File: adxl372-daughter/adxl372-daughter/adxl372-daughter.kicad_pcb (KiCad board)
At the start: 2 copper layers, 30.5 x 23.4 mm, 13 parts, among them J1 Conn_01x08, J2 Conn_01x08, J3 Conn_01x05_Female, J4 Conn_01x05_Female, U1 ADXL372

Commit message: fleshed out daughter card
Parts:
- removed ?: , 
- removed REF** (x4): MountingHole_3mm, MountingHole:MountingHole_3mm
- added H1: MountingHole_3mm_Pad, MountingHole:MountingHole_3mm_Pad, F.Cu at (117.6, 54.1)
- added H2: MountingHole_3mm_Pad, MountingHole:MountingHole_3mm_Pad, F.Cu at (149.1, 54.1)
- added H3: MountingHole_3mm_Pad, MountingHole:MountingHole_3mm_Pad, F.Cu at (149.1, 72.9)
- added H4: MountingHole_3mm_Pad, MountingHole:MountingHole_3mm_Pad, F.Cu at (117.6, 72.9)
- added JP1: SolderJumper_2_Bridged, Jumper:SolderJumper-2_P1.3mm_Bridged2Bar_Pad1.0x1.5mm, F.Cu at (127.5, 63.5)
- added JP2: SolderJumper_3_Bridged12, Jumper:SolderJumper-3_P1.3mm_Bridged2Bar12_Pad1.0x1.5mm, F.Cu at (124.2, 66.0)
- added JP3: SolderJumper_3_Bridged12, Jumper:SolderJumper-3_P1.3mm_Bridged2Bar12_Pad1.0x1.5mm, F.Cu at (124.2, 61.0)
- added R1: 0, Resistor_SMD:R_0603_1608Metric_Pad1.05x0.95mm_HandSolder, F.Cu at (133.9, 67.8)
- added R2: 0, Resistor_SMD:R_0603_1608Metric_Pad1.05x0.95mm_HandSolder, F.Cu at (128.5, 67.8)
- added R3: 0, Resistor_SMD:R_0603_1608Metric_Pad1.05x0.95mm_HandSolder, F.Cu at (130.3, 67.8)
- added R4: 0, Resistor_SMD:R_0603_1608Metric_Pad1.05x0.95mm_HandSolder, F.Cu at (132.1, 67.8)
- moved C3 43.2 mm to (131.1, 59.7), turned to 270 degrees
- moved J3 38.3 mm to (137.4, 58.4)
- moved J4 38.3 mm to (145.0, 58.4)
- moved J2 37.0 mm to (148.8, 63.5)
- moved C2 36.2 mm to (132.8, 59.7)
- moved C1 36.1 mm to (134.6, 59.7)
- moved U1 36.1 mm to (133.3, 63.5)
- moved J1 35.7 mm to (117.8, 63.5)
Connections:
- J4 pad 2: SCLK -> rSCLK
- J4 pad 3: MOSI -> rMOSI
- J4 pad 4: MISO -> rMISO
- J4 pad 5: nCS -> rnCS
- U1 pad 4: SCLK -> rSCLK
- U1 pad 6: MOSI -> rMOSI
- U1 pad 7: MISO -> rMISO
- U1 pad 8: nCS -> rnCS
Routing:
- net rMOSI: track 0.00 -> 39.6 mm, vias 0 -> 1
- net rSCLK: track 0.00 -> 28.2 mm, vias 0 -> 1
- net dnCS: track 0.00 -> 25.9 mm
- net VDD: track 86.5 -> 63.2 mm
- net rMISO: track 0.00 -> 22.7 mm
- net MOSI: track 43.3 -> 65.7 mm
- net INT2: track 10.7 -> 31.2 mm, vias 1 -> 2
- net D1: track 28.6 -> 47.6 mm, vias 2 -> 0
- net GND: track 29.9 -> 11.4 mm, vias 30 -> 10
- net D2: track 29.2 -> 44.8 mm
- net rnCS: track 0.00 -> 15.2 mm
- net SCLK: track 34.5 -> 46.3 mm, vias 3 -> 4
- net MISO: track 39.6 -> 50.6 mm, vias 2 -> 4
- net INT1: track 9.42 -> 19.6 mm
- net nCS: track 44.9 -> 46.3 mm, vias 2 -> 4
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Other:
- board size 30.5 x 23.4 mm -> 38.1 x 25.4 mm
- board text added: "CS"
- board text added: "D1"
- board text added: "D2"
- board text added: "INPUT"
- board text added: "INT1"
- board text added: "INT2"
- board text added: "OUTPUT"
- board text added: "nCS"
- board text removed: "IN"

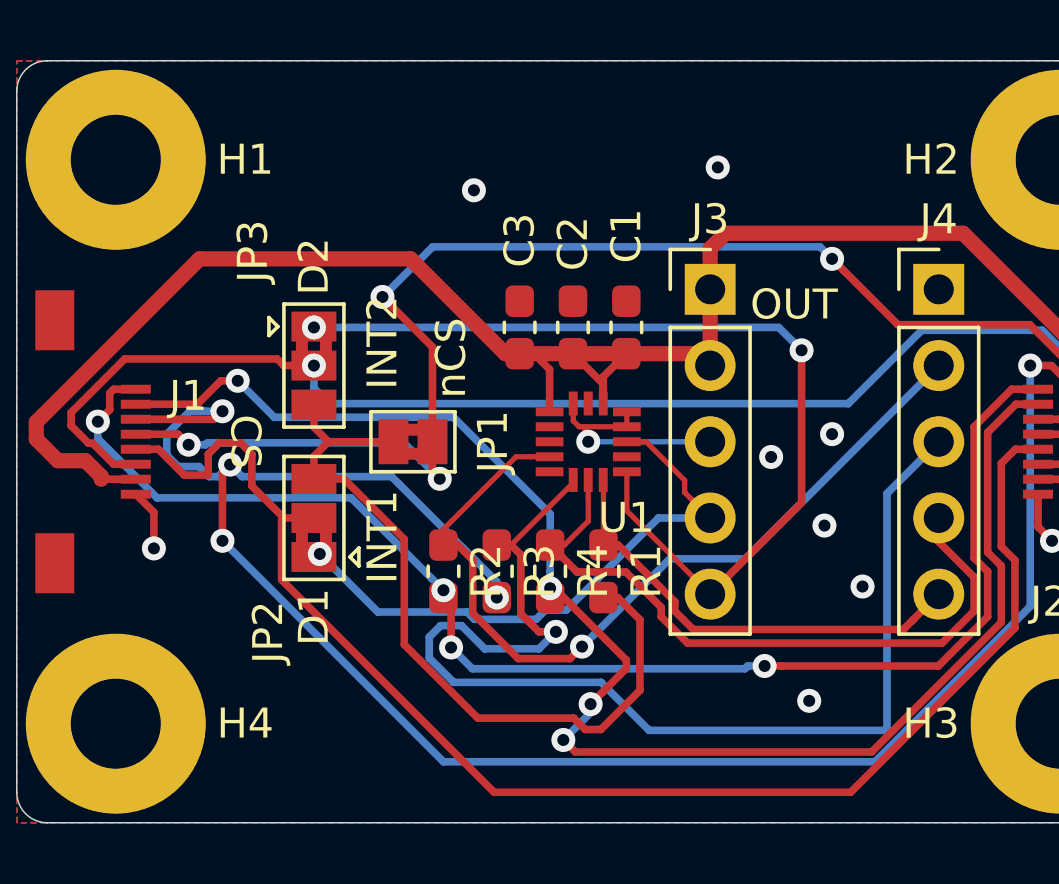
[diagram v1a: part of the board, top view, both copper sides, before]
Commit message: improved ground conectivity
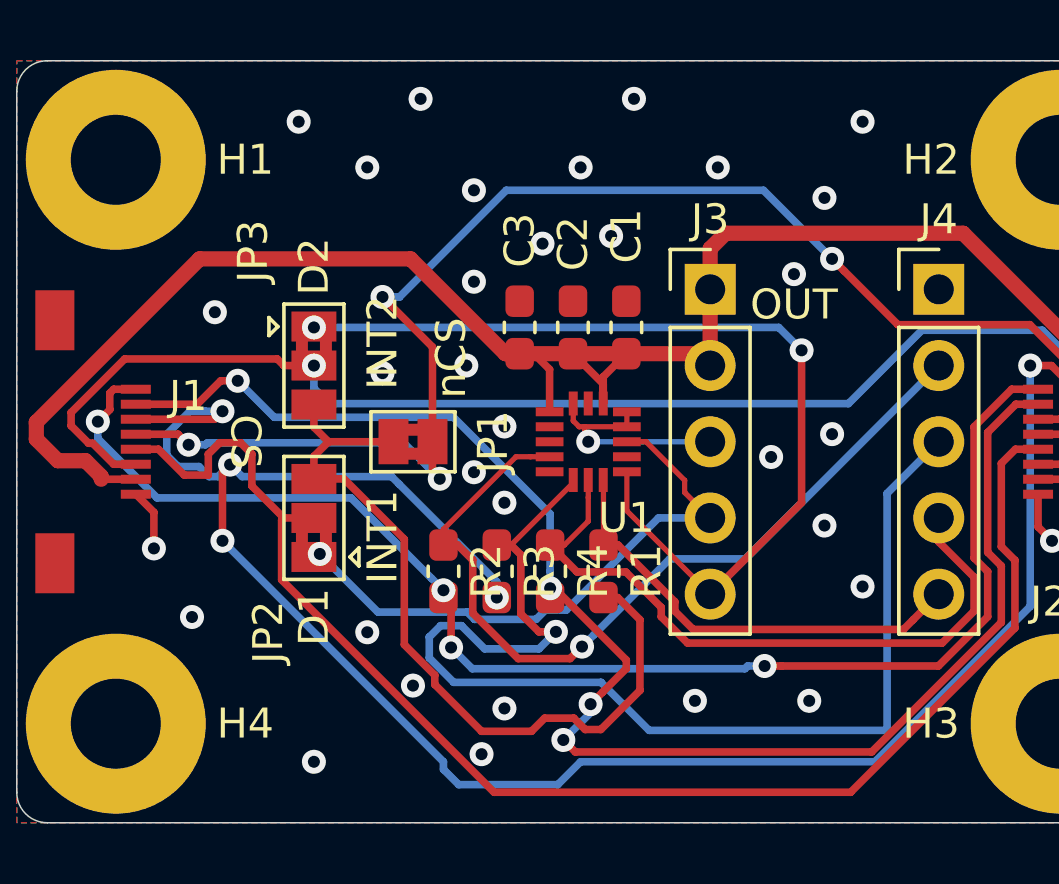
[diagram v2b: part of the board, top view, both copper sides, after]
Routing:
- net nCS: track 46.3 -> 47.9 mm
- net MOSI: track 65.7 -> 66.5 mm
- net dnCS: track 25.9 -> 26.4 mm
- net GND: vias 10 -> 34
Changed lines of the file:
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@@
     (thickness 1.6)
     (drawings 18)
-    (tracks 305)
+    (tracks 339)
     (zones 0)
     (modules 19)
@@
   )
   (setup
-    (last_trace_width 0.25)
+    (last_trace_width 0.254)
     (user_trace_width 0.1524)
     (user_trace_width 0.1778)
@@
     (user_trace_width 0.508)
     (trace_clearance 0.2)
-    (zone_clearance 0.508)
+    (zone_clearance 0.254)
     (zone_45_only no)
     (trace_min 0.1524)
@@
   (gr_arc (start 115.316 75.184) (end 114.3 75.184) (angle -90) (layer Edge.Cuts) (width 0.05))
   (gr_arc (start 151.384 51.816) (end 152.4 51.816) (angle -90) (layer Edge.Cuts) (width 0.05))
+  (via (at 129.54 64.516) (size 0.8) (drill 0.4) (layers F.Cu B.Cu) (net 1))
+  (via (at 130.556 65.532) (size 0.8) (drill 0.4) (layers F.Cu B.Cu) (net 1))
   (segment (start 134.6375 62.5) (end 134.6375 63) (width 0.1778) (layer F.Cu) (net 1))
   (segment (start 132.85 62.8028) (end 132.85 62.225) (width 0.1778) (layer F.Cu) (net 1))
@@
   (via (at 148.80901 66.802) (size 0.8) (drill 0.4) (layers F.Cu B.Cu) (net 1))
   (segment (start 148.344 65.25) (end 148.344 66.33699) (width 0.254) (layer F.Cu) (net 1))
+  (via (at 120.904 59.182) (size 0.8) (drill 0.4) (layers F.Cu B.Cu) (net 1))
+  (via (at 123.698 52.832) (size 0.8) (drill 0.4) (layers F.Cu B.Cu) (net 1))
+  (via (at 125.984 69.85) (size 0.8) (drill 0.4) (layers F.Cu B.Cu) (net 1))
+  (via (at 127.508 71.628) (size 0.8) (drill 0.4) (layers F.Cu B.Cu) (net 1))
+  (via (at 130.556 62.992) (size 0.8) (drill 0.4) (layers F.Cu B.Cu) (net 1))
+  (via (at 129.286 60.96) (size 0.8) (drill 0.4) (layers F.Cu B.Cu) (net 1))
+  (via (at 129.54 58.166) (size 0.8) (drill 0.4) (layers F.Cu B.Cu) (net 1))
+  (via (at 133.096 54.356) (size 0.8) (drill 0.4) (layers F.Cu B.Cu) (net 1))
+  (via (at 127.762 52.07) (size 0.8) (drill 0.4) (layers F.Cu B.Cu) (net 1))
+  (via (at 125.984 54.356) (size 0.8) (drill 0.4) (layers F.Cu B.Cu) (net 1))
+  (via (at 142.494 52.832) (size 0.8) (drill 0.4) (layers F.Cu B.Cu) (net 1))
+  (via (at 141.224 55.372) (size 0.8) (drill 0.4) (layers F.Cu B.Cu) (net 1))
+  (via (at 134.874 52.07) (size 0.8) (drill 0.4) (layers F.Cu B.Cu) (net 1))
+  (via (at 140.208 57.912) (size 0.8) (drill 0.4) (layers F.Cu B.Cu) (net 1))
+  (via (at 134.112 56.642) (size 0.8) (drill 0.4) (layers F.Cu B.Cu) (net 1))
+  (via (at 131.826 56.896) (size 0.8) (drill 0.4) (layers F.Cu B.Cu) (net 1))
+  (via (at 124.206 74.168) (size 0.8) (drill 0.4) (layers F.Cu B.Cu) (net 1))
+  (via (at 120.142 69.342) (size 0.8) (drill 0.4) (layers F.Cu B.Cu) (net 1))
+  (via (at 129.794 73.914) (size 0.8) (drill 0.4) (layers F.Cu B.Cu) (net 1))
+  (via (at 130.556 72.39) (size 0.8) (drill 0.4) (layers F.Cu B.Cu) (net 1))
+  (via (at 136.906 72.136) (size 0.8) (drill 0.4) (layers F.Cu B.Cu) (net 1))
+  (via (at 126.492 61.214) (size 0.8) (drill 0.4) (layers F.Cu B.Cu) (net 1))
   (segment (start 133.85 61.335) (end 134.62 60.565) (width 0.254) (layer F.Cu) (net 2))
   (segment (start 133.85 62.225) (end 133.85 61.335) (width 0.254) (layer F.Cu) (net 2))
@@
   (segment (start 148.082 68.990038) (end 142.904038 74.168) (width 0.254) (layer B.Cu) (net 5))
   (via (at 121.158 66.802) (size 0.8) (drill 0.4) (layers F.Cu B.Cu) (net 5))
-  (segment (start 142.904038 74.168) (end 128.524 74.168) (width 0.254) (layer B.Cu) (net 5))
   (segment (start 128.524 74.168) (end 121.158 66.802) (width 0.254) (layer B.Cu) (net 5))
   (via (at 121.412 64.262) (size 0.8) (drill 0.4) (layers F.Cu B.Cu) (net 5))
@@
   (segment (start 126.795999 64.661999) (end 127.050022 64.916022) (width 0.254) (layer B.Cu) (net 5))
   (segment (start 121.412 64.262) (end 121.811999 64.661999) (width 0.254) (layer B.Cu) (net 5))
+  (segment (start 128.524 74.168) (end 128.524 74.422) (width 0.254) (layer B.Cu) (net 5))
+  (segment (start 128.524 74.422) (end 129.032 74.93) (width 0.254) (layer B.Cu) (net 5))
+  (segment (start 132.334 74.93) (end 133.096 74.168) (width 0.254) (layer B.Cu) (net 5))
+  (segment (start 129.032 74.93) (end 132.334 74.93) (width 0.254) (layer B.Cu) (net 5))
+  (segment (start 142.904038 74.168) (end 133.096 74.168) (width 0.254) (layer B.Cu) (net 5))
   (segment (start 128.158 64.504) (end 128.38901 64.73501) (width 0.254) (layer F.Cu) (net 6))
   (segment (start 128.158 63.5) (end 128.158 64.504) (width 0.254) (layer F.Cu) (net 6))
@@
   (via (at 141.478 57.404) (size 0.8) (drill 0.4) (layers F.Cu B.Cu) (net 6))
   (via (at 126.492 58.674) (size 0.8) (drill 0.4) (layers F.Cu B.Cu) (net 6))
-  (segment (start 128.161999 57.004001) (end 126.492 58.674) (width 0.254) (layer B.Cu) (net 6))
-  (segment (start 141.078001 57.004001) (end 128.161999 57.004001) (width 0.254) (layer B.Cu) (net 6))
-  (segment (start 141.478 57.404) (end 141.078001 57.004001) (width 0.254) (layer B.Cu) (net 6))
   (segment (start 128.158 60.34) (end 128.158 63.5) (width 0.254) (layer F.Cu) (net 6))
   (segment (start 126.492 58.674) (end 128.158 60.34) (width 0.254) (layer F.Cu) (net 6))
@@
   (segment (start 127.200837 63.534999) (end 120.659479 63.534999) (width 0.254) (layer B.Cu) (net 6))
   (segment (start 120.659479 63.534999) (end 120.594555 63.599923) (width 0.254) (layer B.Cu) (net 6))
+  (segment (start 141.478 57.404) (end 139.192 55.118) (width 0.254) (layer B.Cu) (net 6))
+  (segment (start 130.615962 55.118) (end 127.059962 58.674) (width 0.254) (layer B.Cu) (net 6))
+  (segment (start 127.057685 58.674) (end 126.492 58.674) (width 0.254) (layer B.Cu) (net 6))
+  (segment (start 127.059962 58.674) (end 127.057685 58.674) (width 0.254) (layer B.Cu) (net 6))
+  (segment (start 139.192 55.118) (end 130.615962 55.118) (width 0.254) (layer B.Cu) (net 6))
   (segment (start 147.57303 69.709134) (end 142.098164 75.184) (width 0.254) (layer F.Cu) (net 7))
   (segment (start 147.573031 67.450869) (end 147.57303 69.709134) (width 0.254) (layer F.Cu) (net 7))
@@
   (segment (start 124.692 63.5) (end 124.206 63.986) (width 0.254) (layer F.Cu) (net 15))
   (segment (start 126.858 63.5) (end 124.692 63.5) (width 0.254) (layer F.Cu) (net 15))
-  (segment (start 127.219001 70.263039) (end 129.669951 72.713989) (width 0.254) (layer F.Cu) (net 15))
-  (segment (start 132.868787 72.713989) (end 133.246827 73.092029) (width 0.254) (layer F.Cu) (net 15))
   (segment (start 134.333 68.693) (end 133.858 68.693) (width 0.254) (layer F.Cu) (net 15))
   (segment (start 133.77116 73.092029) (end 135.074011 71.789178) (width 0.254) (layer F.Cu) (net 15))
-  (segment (start 124.206 64.74) (end 125.21 64.74) (width 0.254) (layer F.Cu) (net 15))
   (segment (start 135.074011 69.434011) (end 134.333 68.693) (width 0.254) (layer F.Cu) (net 15))
   (segment (start 125.21 64.74) (end 127.219001 66.749001) (width 0.254) (layer F.Cu) (net 15))
+  (segment (start 127.219001 70.263039) (end 128.235001 71.279039) (width 0.254) (layer F.Cu) (net 15))
+  (segment (start 135.074011 71.789178) (end 135.074011 69.434011) (width 0.254) (layer F.Cu) (net 15))
+  (segment (start 131.457978 73.152) (end 131.895989 72.713989) (width 0.254) (layer F.Cu) (net 15))
+  (segment (start 132.868787 72.713989) (end 133.246827 73.092029) (width 0.254) (layer F.Cu) (net 15))
   (segment (start 127.219001 66.749001) (end 127.219001 70.263039) (width 0.254) (layer F.Cu) (net 15))
-  (segment (start 135.074011 71.789178) (end 135.074011 69.434011) (width 0.254) (layer F.Cu) (net 15))
+  (segment (start 124.206 64.74) (end 125.21 64.74) (width 0.254) (layer F.Cu) (net 15))
+  (segment (start 128.235001 71.279039) (end 128.235001 71.593001) (width 0.254) (layer F.Cu) (net 15))
   (segment (start 133.246827 73.092029) (end 133.77116 73.092029) (width 0.254) (layer F.Cu) (net 15))
-  (segment (start 129.669951 72.713989) (end 132.868787 72.713989) (width 0.254) (layer F.Cu) (net 15))
+  (segment (start 128.235001 71.593001) (end 129.794 73.152) (width 0.254) (layer F.Cu) (net 15))
+  (segment (start 129.794 73.152) (end 131.457978 73.152) (width 0.254) (layer F.Cu) (net 15))
+  (segment (start 131.895989 72.713989) (end 132.868787 72.713989) (width 0.254) (layer F.Cu) (net 15))
   (zone (net 1) (net_name GND) (layer B.Cu) (hatch edge 0.508)
-    (connect_pads (clearance 0.508))
-    (min_thickness 0.254)
+    (connect_pads (clearance 0.254))
+    (min_thickness 0.1778)
     (fill yes (arc_segments 32) (thermal_gap 0.508) (thermal_bridge_width 0.508))
     (polygon
@@
   )
   (zone (net 1) (net_name GND) (layer F.Cu) (hatch edge 0.508)
-    (connect_pads (clearance 0.508))
-    (min_thickness 0.254)
+    (connect_pads (clearance 0.254))
+    (min_thickness 0.1778)
     (fill yes (arc_segments 32) (thermal_gap 0.508) (thermal_bridge_width 0.508))
     (polygon

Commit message: make pass drc
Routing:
- net D1: track 47.6 -> 48.9 mm
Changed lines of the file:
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@@
     (thickness 1.6)
     (drawings 18)
-    (tracks 339)
+    (tracks 338)
     (zones 0)
     (modules 19)
@@
   (via (at 123.698 52.832) (size 0.8) (drill 0.4) (layers F.Cu B.Cu) (net 1))
   (via (at 125.984 69.85) (size 0.8) (drill 0.4) (layers F.Cu B.Cu) (net 1))
-  (via (at 127.508 71.628) (size 0.8) (drill 0.4) (layers F.Cu B.Cu) (net 1))
+  (via (at 127.508 71.882) (size 0.8) (drill 0.4) (layers F.Cu B.Cu) (net 1))
   (via (at 130.556 62.992) (size 0.8) (drill 0.4) (layers F.Cu B.Cu) (net 1))
   (via (at 129.286 60.96) (size 0.8) (drill 0.4) (layers F.Cu B.Cu) (net 1))
@@
   (via (at 124.206 74.168) (size 0.8) (drill 0.4) (layers F.Cu B.Cu) (net 1))
   (via (at 120.142 69.342) (size 0.8) (drill 0.4) (layers F.Cu B.Cu) (net 1))
-  (via (at 129.794 73.914) (size 0.8) (drill 0.4) (layers F.Cu B.Cu) (net 1))
+  (via (at 129.286 73.914) (size 0.8) (drill 0.4) (layers F.Cu B.Cu) (net 1))
   (via (at 130.556 72.39) (size 0.8) (drill 0.4) (layers F.Cu B.Cu) (net 1))
   (via (at 136.906 72.136) (size 0.8) (drill 0.4) (layers F.Cu B.Cu) (net 1))
@@
   (segment (start 127.059962 58.674) (end 127.057685 58.674) (width 0.254) (layer B.Cu) (net 6))
   (segment (start 139.192 55.118) (end 130.615962 55.118) (width 0.254) (layer B.Cu) (net 6))
-  (segment (start 147.57303 69.709134) (end 142.098164 75.184) (width 0.254) (layer F.Cu) (net 7))
-  (segment (start 147.573031 67.450869) (end 147.57303 69.709134) (width 0.254) (layer F.Cu) (net 7))
-  (segment (start 147.119022 66.996861) (end 147.573031 67.450869) (width 0.254) (layer F.Cu) (net 7))
-  (segment (start 147.119022 64.220978) (end 147.119022 66.996861) (width 0.254) (layer F.Cu) (net 7))
-  (segment (start 148.344 63.75) (end 147.59 63.75) (width 0.254) (layer F.Cu) (net 7))
-  (segment (start 147.59 63.75) (end 147.119022 64.220978) (width 0.254) (layer F.Cu) (net 7))
-  (segment (start 123.128999 68.101601) (end 123.128999 66.113001) (width 0.254) (layer F.Cu) (net 7))
   (segment (start 123.202 66.04) (end 124.206 66.04) (width 0.254) (layer F.Cu) (net 7))
-  (segment (start 123.128999 66.113001) (end 123.202 66.04) (width 0.254) (layer F.Cu) (net 7))
-  (segment (start 130.211398 75.184) (end 123.128999 68.101601) (width 0.254) (layer F.Cu) (net 7))
-  (segment (start 142.098164 75.184) (end 130.211398 75.184) (width 0.254) (layer F.Cu) (net 7))
   (segment (start 120.684998 63.913038) (end 121.063038 63.534998) (width 0.254) (layer F.Cu) (net 7))
   (segment (start 120.684998 64.610962) (end 120.684998 63.913038) (width 0.254) (layer F.Cu) (net 7))
@@
   (segment (start 118.27 63.75) (end 119.024 63.75) (width 0.254) (layer F.Cu) (net 7))
   (segment (start 122.139002 63.913038) (end 122.139002 64.977002) (width 0.254) (layer F.Cu) (net 7))
+  (segment (start 128.016 75.184) (end 123.128999 70.296999) (width 0.254) (layer F.Cu) (net 7))
+  (segment (start 142.098164 75.184) (end 128.016 75.184) (width 0.254) (layer F.Cu) (net 7))
+  (segment (start 147.57303 69.709134) (end 142.098164 75.184) (width 0.254) (layer F.Cu) (net 7))
+  (segment (start 147.119022 66.996861) (end 147.573031 67.450869) (width 0.254) (layer F.Cu) (net 7))
+  (segment (start 123.128999 66.113001) (end 123.202 66.04) (width 0.254) (layer F.Cu) (net 7))
+  (segment (start 123.128999 70.296999) (end 123.128999 66.113001) (width 0.254) (layer F.Cu) (net 7))
+  (segment (start 147.59 63.75) (end 147.119022 64.220978) (width 0.254) (layer F.Cu) (net 7))
+  (segment (start 147.119022 64.220978) (end 147.119022 66.996861) (width 0.254) (layer F.Cu) (net 7))
+  (segment (start 148.344 63.75) (end 147.59 63.75) (width 0.254) (layer F.Cu) (net 7))
+  (segment (start 147.573031 67.450869) (end 147.57303 69.709134) (width 0.254) (layer F.Cu) (net 7))
   (segment (start 116.112998 62.526332) (end 117.898332 60.740998) (width 0.254) (layer F.Cu) (net 8))
   (segment (start 116.832546 63.551148) (end 116.69682 63.551148) (width 0.254) (layer F.Cu) (net 8))
@@
   (segment (start 137.414 66.04) (end 135.691182 66.04) (width 0.254) (layer B.Cu) (net 10))
   (segment (start 129.315018 69.176988) (end 126.339136 69.176988) (width 0.254) (layer B.Cu) (net 10))
-  (segment (start 130.942 64) (end 131.4222 64) (width 0.1778) (layer F.Cu) (net 11))
-  (segment (start 131.4222 64) (end 132.0625 64) (width 0.1778) (layer F.Cu) (net 11))
-  (segment (start 128.524 66.418) (end 130.942 64) (width 0.1778) (layer F.Cu) (net 11))
-  (segment (start 128.524 66.943) (end 128.524 66.418) (width 0.1778) (layer F.Cu) (net 11))
   (segment (start 132.742707 70.729193) (end 133.142706 70.329194) (width 0.254) (layer F.Cu) (net 11))
   (via (at 133.142706 70.329194) (size 0.8) (drill 0.4) (layers F.Cu B.Cu) (net 11))
@@
   (segment (start 138.591001 67.402999) (end 136.068901 67.402999) (width 0.254) (layer B.Cu) (net 11))
   (segment (start 128.524 66.943) (end 128.999 66.943) (width 0.254) (layer F.Cu) (net 11))
+  (segment (start 131.075574 64) (end 132.0625 64) (width 0.1778) (layer F.Cu) (net 11))
+  (segment (start 128.524 66.943) (end 128.524 66.551574) (width 0.1778) (layer F.Cu) (net 11))
+  (segment (start 128.524 66.551574) (end 131.075574 64) (width 0.1778) (layer F.Cu) (net 11))
   (segment (start 132.85 64.87) (end 132.85 64.775) (width 0.1778) (layer F.Cu) (net 12))
   (segment (start 130.777 66.943) (end 132.85 64.87) (width 0.1778) (layer F.Cu) (net 12))
